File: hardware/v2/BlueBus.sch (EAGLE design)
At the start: 149 parts, among them J1 TC2030, Q1 NMOSFET-BSS138K, Q2 PMOSFET-DMP32D4SSOT323, Q3 NMOSFET-BSS138K

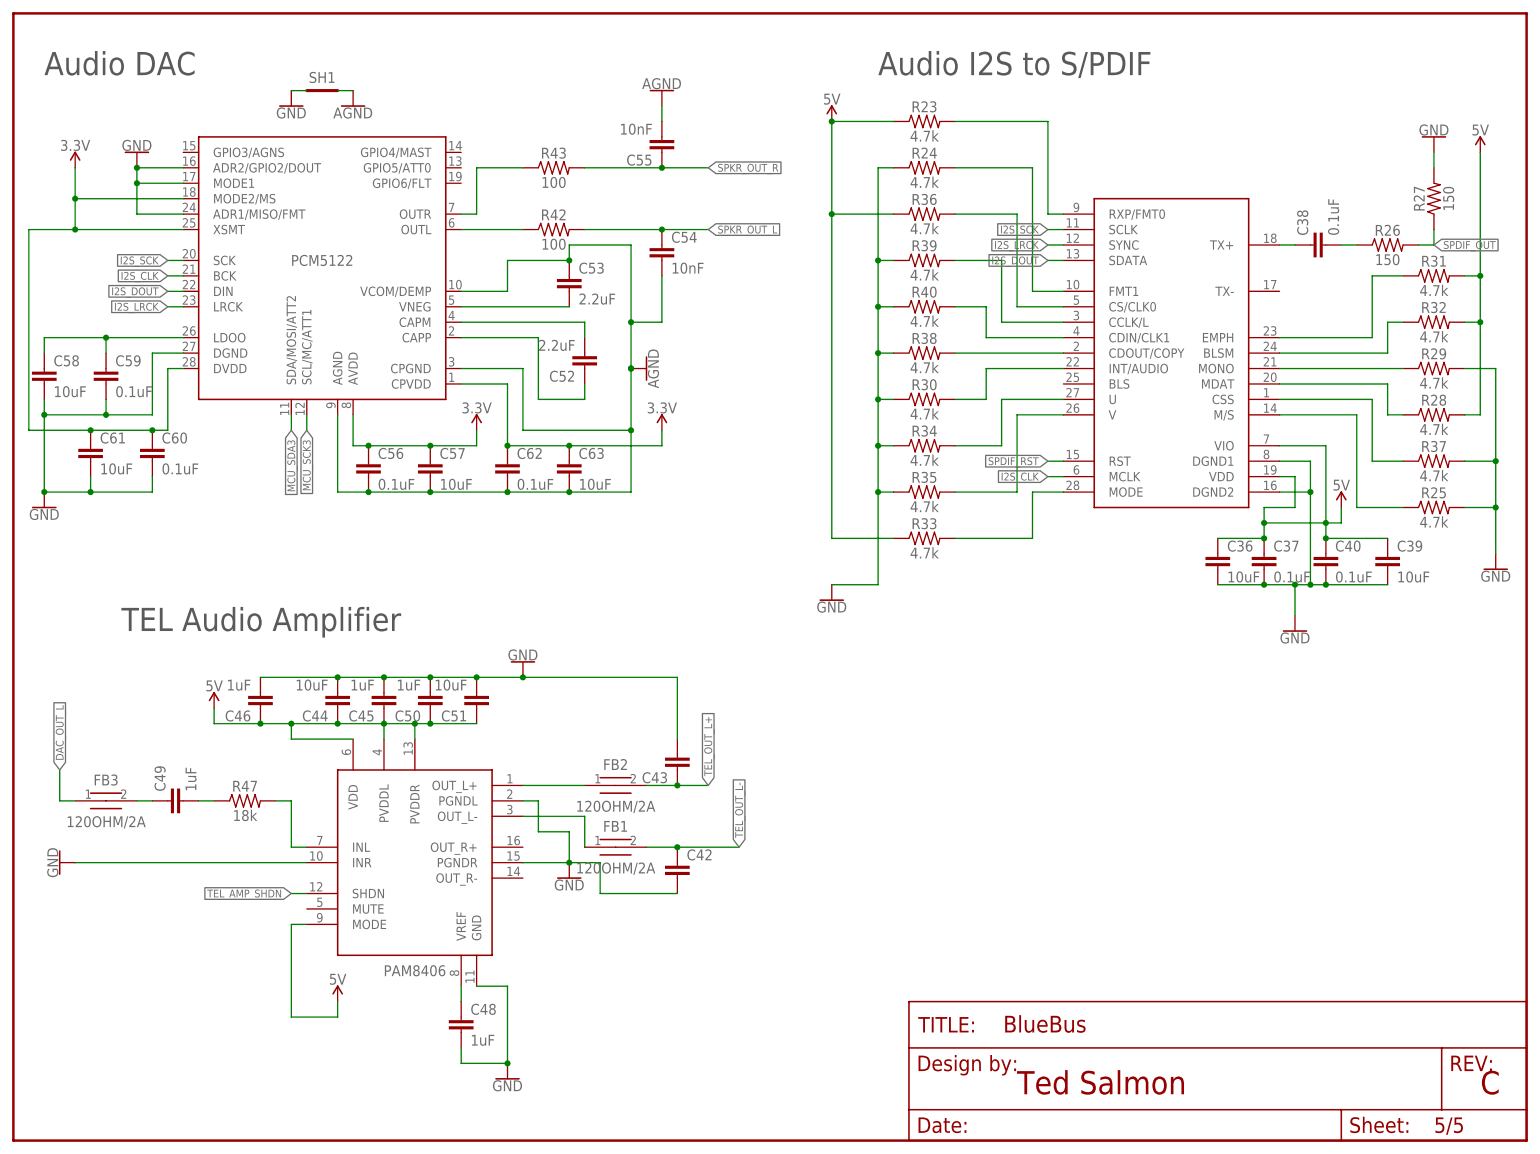
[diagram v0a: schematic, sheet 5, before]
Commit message: [IMP] hardware: V2 Improvements * Increase the footprint for C1 and fix the name location * Remove PU/PD resistors from DIT4096 * Rewire I2S lines * Fix ground pour polygon dimensions * Replace 10ohm resistor for two parallel 20ohm * Wire SMB ground to unfiltered ground * Rename all connectors and ICs per convention * Increase name size to 1mm at minimum * Add additional ground VIAs
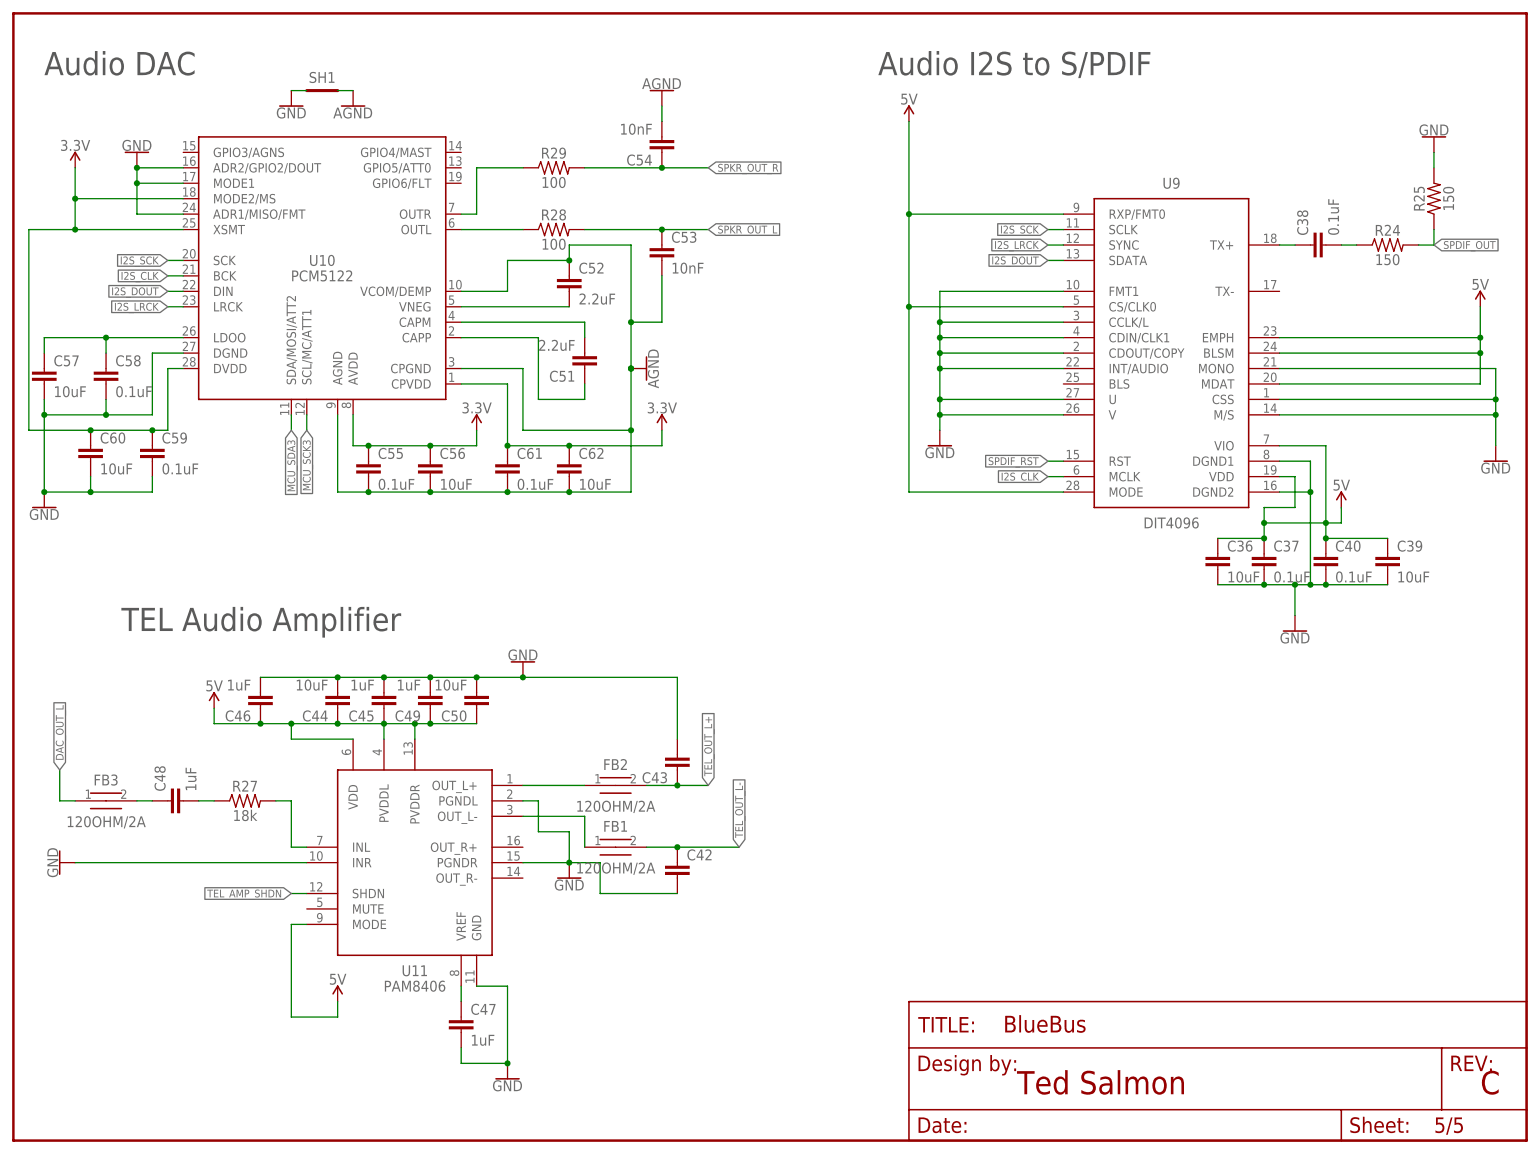
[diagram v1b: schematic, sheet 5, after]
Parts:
- removed C63: 10uF, Passives:10UF0603
- removed PWR_IN: 3PIN_953442_1, Connectors:3PIN_953442_1
- removed R30, R31, R32, R33, R34, R35, R36, R37, R38, R39, R40: 4.7k, Passives:4.7KOHM0603
- removed R41: 10k, Passives:10KOHM0603
- removed R42, R43: 100, Passives:100OHM0603
- removed R47: 18k, Passives:18KOHM0603
- added C47: 1uF, Passives:1UF0603
- added J8: TC2030, Connectors:TC2030
- C22: device Passives:47NF -> Passives:47NF0603
- C23: value 100PF -> 100pF; device Passives:100PF -> Passives:100PF0603
- C50: value 1uF -> 10uF; device Passives:1UF0603 -> Passives:10UF0603
- C51: value 10uF -> 2.2uF; device Passives:10UF0603 -> Passives:2.2UF0603
- C53: value 2.2uF -> 10nF; device Passives:2.2UF0603 -> Passives:10NF0603
- C55: value 10nF -> 0.1uF; device Passives:10NF0603 -> Passives:0.1UF0603
- C56, C60, C62: value 0.1uF -> 10uF; device Passives:0.1UF0603 -> Passives:10UF0603
- C58, C61: value 10uF -> 0.1uF; device Passives:10UF0603 -> Passives:0.1UF0603
- J1: value TC2030 -> 3PIN_953442_1; device Connectors:TC2030 -> Connectors:3PIN_953442_1
- R17: value 10 -> 20; device Passives:10OHM -> Passives:20OHM0603
- R18: value 2k -> 20; device Passives:2KOHM0603 -> Passives:20OHM0603
- R21: value 1k -> 2k; device Passives:1KOHM0603 -> Passives:2KOHM0603
- R23: value 4.7k -> 1k; device Passives:4.7KOHM0603 -> Passives:1KOHM0603
- R24, R25: value 4.7k -> 150; device Passives:4.7KOHM0603 -> Passives:150OHM0603
- R26: value 150 -> 10k; device Passives:150OHM0603 -> Passives:10KOHM0603
- R27: value 150 -> 18k; device Passives:150OHM0603 -> Passives:18KOHM0603
- R28, R29: value 4.7k -> 100; device Passives:4.7KOHM0603 -> Passives:100OHM0603
- renumbered BM83 to U8, CAT25M01 to U6, DIT4096 to U9, DSP_OUT to J5, FT231X to U3, MIC_IN to J4, MPQ4420 to U1, PAM8406 to U11, PCM5122 to U10, PIC24FJ1024GA606 to U7, RECOVERY to J7, S1212BC0 to U4, SPKR_OUT to J2, TCU_IO to J3, TH3122 to U2, USB to J6, XC6210 to U5
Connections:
- removed net SPDIF_AUDIO: R30.2, U9.INT/AUDIO
- removed net SPDIF_BLSM: R32.1, U9.BLSM
- removed net SPDIF_CLK0: R36.2, U9.CS/CLK0
- removed net SPDIF_CLK1: R40.2, U9.CDIN/CLK1
- removed net SPDIF_COPY: R38.2, U9.CDOUT/COPY
- removed net SPDIF_CSS: R37.1, U9.CSS
- removed net SPDIF_EMPH: R31.1, U9.EMPH
- removed net SPDIF_FMT0: R23.2, U9.RXP/FMT0
- removed net SPDIF_FMT1: R24.2, U9.FMT1
- removed net SPDIF_L: R39.2, U9.CCLK/L
- removed net SPDIF_MDAT: R28.1, U9.MDAT
- removed net SPDIF_MODE: R33.2, U9.MODE
- removed net SPDIF_MONO: R29.1, U9.MONO
- removed net SPDIF_MS: R25.1, U9.M/S
- removed net SPDIF_U: R34.2, U9.U
- removed net SPDIF_V: R35.2, U9.V
- net 12V: now also R26.1; no longer R41.1
- net 3.3V: now also C55.1, C59.1, J8.2; no longer C57.1, C63.1, J1.2
- net 5V: now also C49.1, U9.BLSM, U9.CS/CLK0, U9.EMPH, U9.MDAT, U9.MODE, U9.RXP/FMT0; no longer C51.1, R23.1, R28.2, R31.2, R32.2, R33.1, R36.1
- net AGND: now also C52.1, C53.2, C61.2; no longer C53.1, C57.2, C63.2
- net BT_MIC_L: now also R23.1; no longer R22.1
- net DAC_CAPM: now also C51.2; no longer C52.2
- net DAC_CAPP: now also C51.1; no longer C52.1
- net DAC_LDOO: now also C57.1; no longer C59.1
- net DAC_OUT_L: now also R28.1; no longer R42.1
- net DAC_OUT_R: now also R29.1; no longer R43.1
- net DAC_VNEG: now also C52.2; no longer C53.2
- net GND: now also C47.2, C49.2, C57.2, J7.GND, J8.3, U9.CCLK/L, U9.CDIN/CLK1, U9.CDOUT/COPY, U9.CSS, U9.FMT1, U9.INT/AUDIO, U9.M/S, U9.MONO, U9.U, U9.V; no longer C48.2, C51.2, C61.2, J1.3, J5.GND, R24.1, R27.2, R29.2, R30.1, R34.1, R35.1, R37.2, R38.1, R39.1, R40.1
- net GND_FLT: now also J1.1, J5.GND; no longer PWR_IN.1
- net IBUS: now also J1.3, R18.1; no longer PWR_IN.3
- net IBUS_FILT: now also R18.2
- net MCU_MCLR: now also J8.1; no longer J1.1
- net MCU_ON_LED: now also R21.2; no longer R20.2
- net MCU_ON_LED_RES: now also R21.1; no longer R20.1
- net MCU_PGC: now also J8.5; no longer J1.5
- net MCU_PGD: now also J8.4; no longer J1.4
- net MICP1_RES: now also R22.1, R23.2; no longer R21.1, R22.2
- net MIC_BIAS: now also R22.2; no longer R21.2
- net SPDIF_OUT: now also R24.2, R25.1; no longer R26.2, R27.1
- net SPDIF_TX_RES: now also R24.1; no longer R26.1
- net SPKR_OUT_L: now also C53.1, R28.2; no longer C54.1, R42.2
- net SPKR_OUT_R: now also C54.1, R29.2; no longer C55.1, R43.2
- net SYS_RX_LED: now also R20.2; no longer R19.2
- net SYS_RX_LED_RES: now also R20.1; no longer R19.1
- net SYS_TX_LED: now also R19.2; no longer R18.2
- net SYS_TX_LED_RES: now also R19.1; no longer R18.1
- net TEL_AMP_IN: now also C48.1; no longer C49.1
- net TEL_AMP_INL: now also R27.2; no longer R47.2
- net TEL_AMP_INL_CAP_RES: now also C48.2, R27.1; no longer C49.2, R47.1
- net TEL_AMP_VREF: now also C47.1; no longer C48.1
- net TEL_MIC_L_OUT: now also R26.2; no longer R41.2
- net VBAT: now also J1.2; no longer PWR_IN.2
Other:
- moved on the sheet: C48, C49, C50, C51, C52, C53, C54, C55, C56, C57, C58, C59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

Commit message: Stuff
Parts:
- U4: value S-1212BC0-M5T1U -> S-1212BC0-U5T1U; device ICs:S-1212BC0-M5T1U -> ICs:S-1212BC0U5T1
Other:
- moved on the sheet: C3, C4, U4
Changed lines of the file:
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@@
 <part name="L2" library="Passives" deviceset="MPL-SE5040-100" device="" value="10uH"/>
 <part name="C1" library="Passives" deviceset="RHS1V101MCN1GS" device=""/>
-<part name="U4" library="ICs" deviceset="S-1212BC0-M5T1U" device="" value="S-1212BC0-M5T1U"/>
 <part name="C4" library="Passives" deviceset="1UF" device="0603" value="1uF"/>
 <part name="C3" library="Passives" deviceset="2.2UF" device="0603" value="2.2uF"/>
@@
 <part name="R17" library="Passives" deviceset="20OHM" device="0603" value="20"/>
 <part name="R18" library="Passives" deviceset="20OHM" device="0603" value="20"/>
+<part name="U4" library="ICs" deviceset="S-1212BC0" device="U5T1" value="S-1212BC0-U5T1U"/>
+<part name="GND30" library="SparkFun-PowerSymbols" library_urn="urn:adsk.eagle:library:530" deviceset="GND" device=""/>
 </parts>
 <sheets>
@@
 <attribute name="VALUE" x="43.18" y="134.366" size="1.778" layer="96" align="top-center"/>
 </instance>
-<instance part="SUPPLY16" gate="G$1" x="154.94" y="177.8" smashed="yes">
-<attribute name="VALUE" x="154.94" y="180.594" size="1.778" layer="96" align="bottom-center"/>
+<instance part="SUPPLY16" gate="G$1" x="152.4" y="170.18" smashed="yes">
+<attribute name="VALUE" x="152.4" y="172.974" size="1.778" layer="96" align="bottom-center"/>
 </instance>
 <instance part="GND16" gate="1" x="109.22" y="127" smashed="yes">
@@
 <attribute name="VALUE" x="26.924" y="84.201" size="1.778" layer="96" font="vector"/>
 </instance>
-<instance part="U4" gate="G$1" x="167.64" y="152.4" smashed="yes">
-<attribute name="NAME" x="167.64" y="158.75" size="1.778" layer="95" font="vector" align="bottom-center"/>
-<attribute name="VALUE" x="167.64" y="144.78" size="1.778" layer="96" align="center"/>
-</instance>
-<instance part="C4" gate="G$1" x="149.86" y="149.86" smashed="yes">
-<attribute name="NAME" x="151.384" y="152.781" size="1.778" layer="95" font="vector"/>
-<attribute name="VALUE" x="151.384" y="147.701" size="1.778" layer="96" font="vector"/>
-</instance>
-<instance part="C3" gate="G$1" x="182.88" y="149.86" smashed="yes">
-<attribute name="NAME" x="184.404" y="152.781" size="1.778" layer="95" font="vector"/>
-<attribute name="VALUE" x="184.404" y="147.701" size="1.778" layer="96" font="vector"/>
-</instance>
-<instance part="GND36" gate="1" x="167.64" y="139.7" smashed="yes">
-<attribute name="VALUE" x="167.64" y="139.446" size="1.778" layer="96" align="top-center"/>
+<instance part="C4" gate="G$1" x="152.4" y="160.02" smashed="yes">
+<attribute name="NAME" x="153.924" y="162.941" size="1.778" layer="95" font="vector"/>
+<attribute name="VALUE" x="153.924" y="157.861" size="1.778" layer="96" font="vector"/>
+</instance>
+<instance part="C3" gate="G$1" x="190.5" y="160.02" smashed="yes">
+<attribute name="NAME" x="192.024" y="162.941" size="1.778" layer="95" font="vector"/>
+<attribute name="VALUE" x="192.024" y="157.861" size="1.778" layer="96" font="vector"/>
+</instance>
+<instance part="GND36" gate="1" x="157.48" y="147.32" smashed="yes">
+<attribute name="VALUE" x="157.48" y="147.066" size="1.778" layer="96" align="top-center"/>
 </instance>
 <instance part="U3" gate="U$1" x="45.72" y="96.52" smashed="yes">
@@
 <attribute name="VALUE" x="7.62" y="98.806" size="1.778" layer="96" align="top-center"/>
 </instance>
-<instance part="SUPPLY27" gate="G$1" x="154.94" y="147.32" smashed="yes" rot="R180">
-<attribute name="VALUE" x="154.94" y="144.526" size="1.778" layer="96" rot="R180" align="bottom-center"/>
+<instance part="SUPPLY27" gate="G$1" x="160.02" y="170.18" smashed="yes">
+<attribute name="VALUE" x="160.02" y="172.974" size="1.778" layer="96" align="bottom-center"/>
 </instance>
 <instance part="U6" gate="G$1" x="200.66" y="93.98" smashed="yes">
@@
 <attribute name="NAME" x="10.16" y="24.384" size="1.778" layer="95" font="vector" align="bottom-center"/>
 <attribute name="VALUE" x="10.16" y="21.336" size="1.778" layer="96" font="vector" align="top-center"/>
+</instance>
+<instance part="U4" gate="G$1" x="172.72" y="162.56" smashed="yes">
+<attribute name="NAME" x="172.72" y="168.91" size="1.778" layer="95" font="vector" align="bottom-center"/>
+<attribute name="VALUE" x="172.72" y="154.94" size="1.778" layer="96" align="center"/>
+</instance>
+<instance part="GND30" gate="1" x="190.5" y="147.32" smashed="yes">
+<attribute name="VALUE" x="190.5" y="147.066" size="1.778" layer="96" align="top-center"/>
 </instance>
 </instances>
@@
 <segment>
 <pinref part="U4" gate="G$1" pin="GND"/>
-<wire x1="157.48" y1="152.4" x2="152.4" y2="152.4" width="0.1524" layer="91"/>
-<wire x1="152.4" y1="152.4" x2="152.4" y2="142.24" width="0.1524" layer="91"/>
-<wire x1="152.4" y1="142.24" x2="167.64" y2="142.24" width="0.1524" layer="91"/>
+<wire x1="162.56" y1="162.56" x2="157.48" y2="162.56" width="0.1524" layer="91"/>
+<wire x1="157.48" y1="162.56" x2="157.48" y2="154.94" width="0.1524" layer="91"/>
+<pinref part="C4" gate="G$1" pin="2"/>
+<wire x1="152.4" y1="157.48" x2="152.4" y2="154.94" width="0.1524" layer="91"/>
+<wire x1="152.4" y1="154.94" x2="157.48" y2="154.94" width="0.1524" layer="91"/>
 <pinref part="GND36" gate="1" pin="GND"/>
+<wire x1="157.48" y1="149.86" x2="157.48" y2="154.94" width="0.1524" layer="91"/>
+<junction x="157.48" y="154.94"/>
+</segment>
+<segment>
 <pinref part="C3" gate="G$1" pin="2"/>
-<wire x1="182.88" y1="142.24" x2="182.88" y2="147.32" width="0.1524" layer="91"/>
-<wire x1="182.88" y1="142.24" x2="167.64" y2="142.24" width="0.1524" layer="91"/>
-<junction x="167.64" y="142.24"/>
-<pinref part="C4" gate="G$1" pin="2"/>
-<wire x1="149.86" y1="147.32" x2="149.86" y2="142.24" width="0.1524" layer="91"/>
-<wire x1="149.86" y1="142.24" x2="152.4" y2="142.24" width="0.1524" layer="91"/>
-<junction x="152.4" y="142.24"/>
+<pinref part="GND30" gate="1" pin="GND"/>
+<wire x1="190.5" y1="157.48" x2="190.5" y2="149.86" width="0.1524" layer="91"/>
 </segment>
 </net>
@@
 </segment>
 <segment>
+<pinref part="U4" gate="G$1" pin="VIN"/>
 <pinref part="C4" gate="G$1" pin="1"/>
-<wire x1="157.48" y1="154.94" x2="149.86" y2="154.94" width="0.1524" layer="91"/>
-<junction x="149.86" y="154.94"/>
+<wire x1="162.56" y1="165.1" x2="152.4" y2="165.1" width="0.1524" layer="91"/>
 <pinref part="SUPPLY16" gate="G$1" pin="VIN"/>
-<wire x1="149.86" y1="154.94" x2="149.86" y2="177.8" width="0.1524" layer="91"/>
-<wire x1="149.86" y1="177.8" x2="154.94" y2="177.8" width="0.1524" layer="91"/>
-<pinref part="U4" gate="G$1" pin="VIN"/>
+<wire x1="152.4" y1="170.18" x2="152.4" y2="165.1" width="0.1524" layer="91"/>
+<junction x="152.4" y="165.1"/>
 </segment>
 </net>
@@
 <net name="12V" class="3">
 <segment>
-<pinref part="Q2" gate="G$1" pin="S"/>
-<wire x1="124.46" y1="147.32" x2="124.46" y2="149.86" width="0.1524" layer="91"/>
-<pinref part="R3" gate="G$1" pin="2"/>
-<wire x1="124.46" y1="147.32" x2="121.92" y2="147.32" width="0.1524" layer="91"/>
-<junction x="124.46" y="147.32"/>
-<pinref part="U4" gate="G$1" pin="VOUT"/>
-<wire x1="144.78" y1="147.32" x2="124.46" y2="147.32" width="0.1524" layer="91"/>
-<wire x1="177.8" y1="154.94" x2="182.88" y2="154.94" width="0.1524" layer="91"/>
-<wire x1="182.88" y1="154.94" x2="193.04" y2="154.94" width="0.1524" layer="91"/>
-<wire x1="193.04" y1="154.94" x2="193.04" y2="137.16" width="0.1524" layer="91"/>
-<wire x1="193.04" y1="137.16" x2="144.78" y2="137.16" width="0.1524" layer="91"/>
-<wire x1="144.78" y1="137.16" x2="144.78" y2="147.32" width="0.1524" layer="91"/>
-<pinref part="C3" gate="G$1" pin="1"/>
-<junction x="182.88" y="154.94"/>
-</segment>
-<segment>
 <pinref part="R26" gate="G$1" pin="1"/>
 <wire x1="203.2" y1="160.02" x2="203.2" y2="165.1" width="0.1524" layer="91"/>
 <label x="203.2" y="165.1" size="1.778" layer="95"/>
+</segment>
+<segment>
+<pinref part="U4" gate="G$1" pin="VOUT"/>
+<pinref part="C3" gate="G$1" pin="1"/>
+<wire x1="182.88" y1="165.1" x2="190.5" y2="165.1" width="0.1524" layer="91"/>
+<label x="190.5" y="165.1" size="1.27" layer="95" rot="R90" xref="yes"/>
+</segment>
+<segment>
+<pinref part="R3" gate="G$1" pin="2"/>
+<pinref part="Q2" gate="G$1" pin="S"/>
+<wire x1="124.46" y1="147.32" x2="124.46" y2="149.86" width="0.1524" layer="91"/>
+<wire x1="124.46" y1="147.32" x2="121.92" y2="147.32" width="0.1524" layer="91"/>
+<label x="124.46" y="147.32" size="1.27" layer="95" xref="yes"/>
 </segment>
 </net>
@@
 <segment>
 <pinref part="U4" gate="G$1" pin="CE"/>
-<wire x1="154.94" y1="149.86" x2="157.48" y2="149.86" width="0.1524" layer="91"/>
-<wire x1="154.94" y1="149.86" x2="154.94" y2="147.32" width="0.1524" layer="91"/>
+<wire x1="162.56" y1="160.02" x2="160.02" y2="160.02" width="0.1524" layer="91"/>
 <pinref part="SUPPLY27" gate="G$1" pin="5V"/>
-</segment>
-</net>
+<wire x1="160.02" y1="160.02" x2="160.02" y2="170.18" width="0.1524" layer="91"/>
+</segment>
+</net>
